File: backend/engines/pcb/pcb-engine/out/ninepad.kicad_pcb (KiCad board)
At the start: 2 copper layers, 60.3 x 82 mm, 14 parts, among them SW1 1, SW2 2, SW3 4, SW4 5, SW5 6, SW6 7, SW7 8, SW8 9, U1 XIAO RP2040

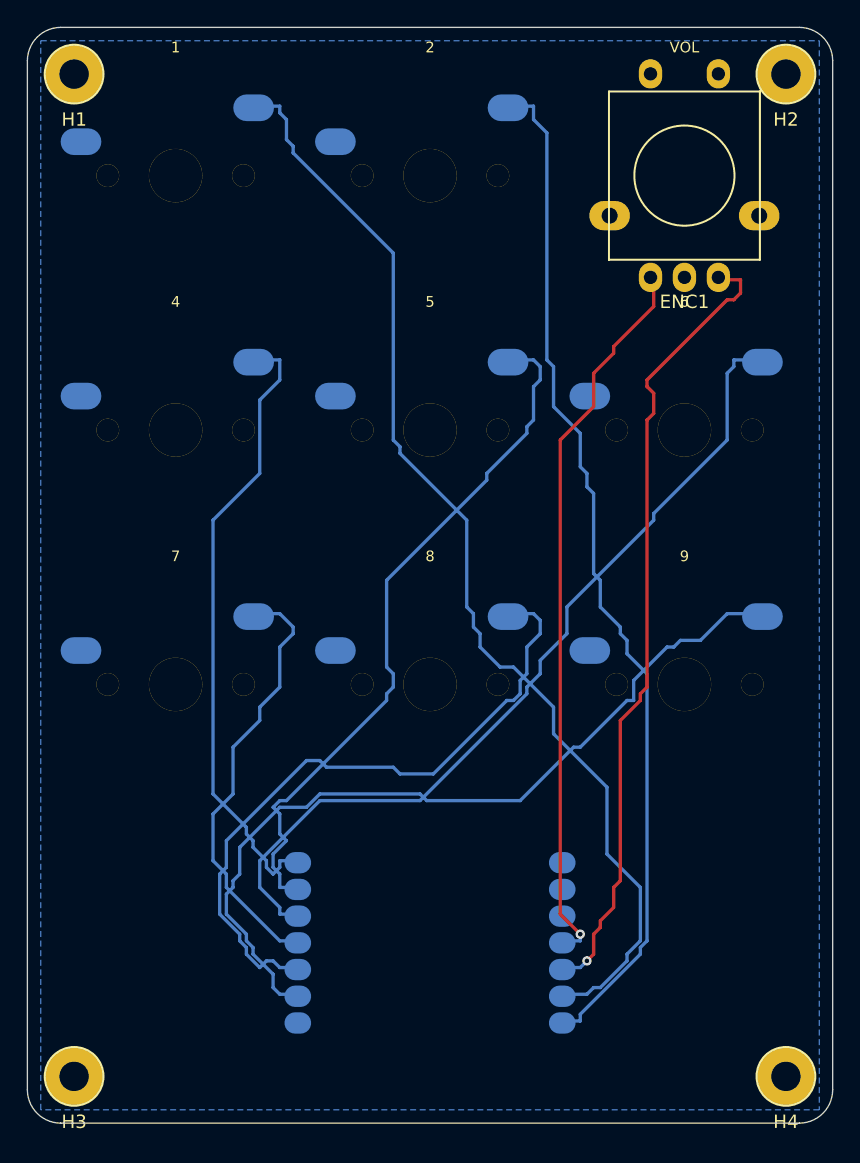
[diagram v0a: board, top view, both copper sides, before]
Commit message: case compiler: pcb result -> parametric openscad. xiao flipped 180 so usb faces the board edge. job #2 (ninepad) end to end with case artifacts. openscad-verified stls for all reference boards
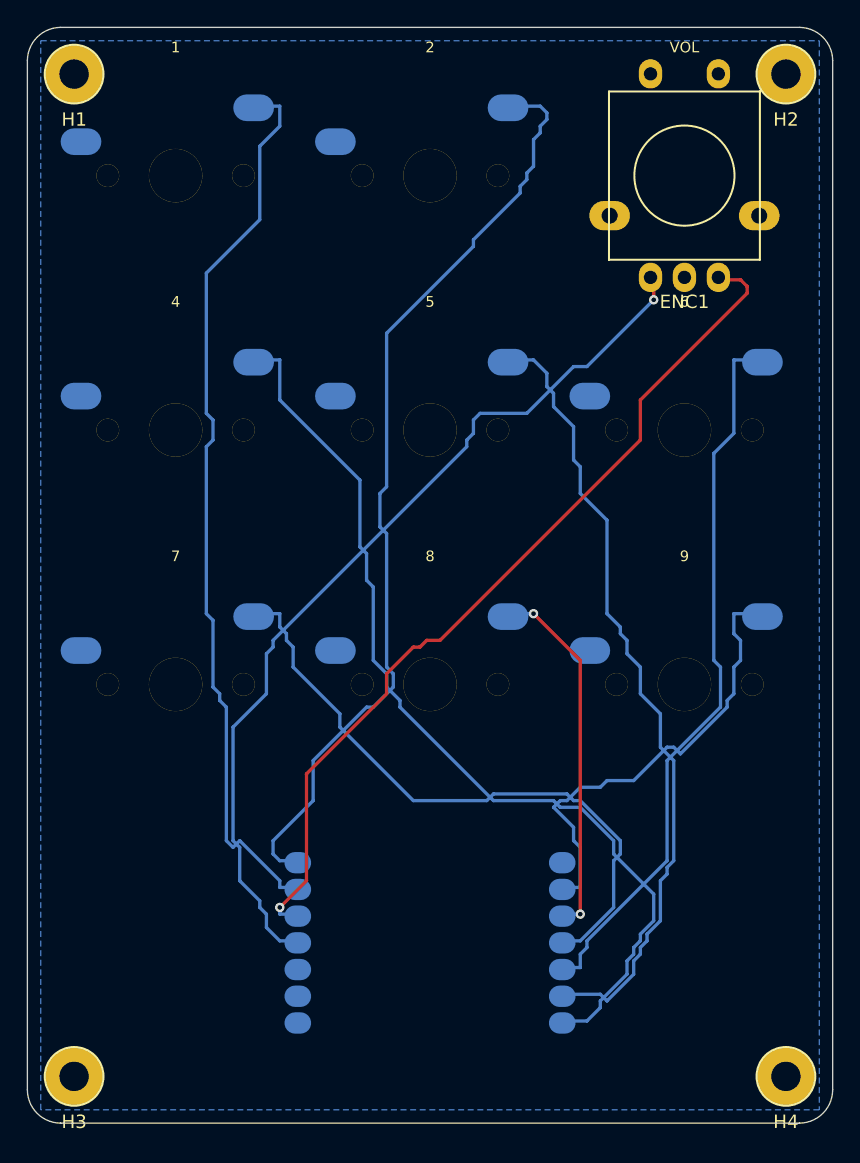
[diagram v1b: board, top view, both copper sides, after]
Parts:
- turned U1 to -180 degrees
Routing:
- net K8: track 62.1 -> 34.5 mm
- net K3: track 47.1 -> 70.7 mm
- net K7: track 50.6 -> 27.4 mm, vias 0 -> 2
- net K1: track 84.2 -> 68.0 mm
- net K6: track 33.0 -> 47.5 mm
- net ENC1_A: track 54.5 -> 68.1 mm
- net K5: track 64.7 -> 54.2 mm
- net K2: track 77.6 -> 70.5 mm
- net K4: track 53.2 -> 60.1 mm
- net ENC1_B: track 60.2 -> 66.1 mm
